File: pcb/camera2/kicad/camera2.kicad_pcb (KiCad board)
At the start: 4 copper layers, 96.5 x 45.7 mm, 63 parts

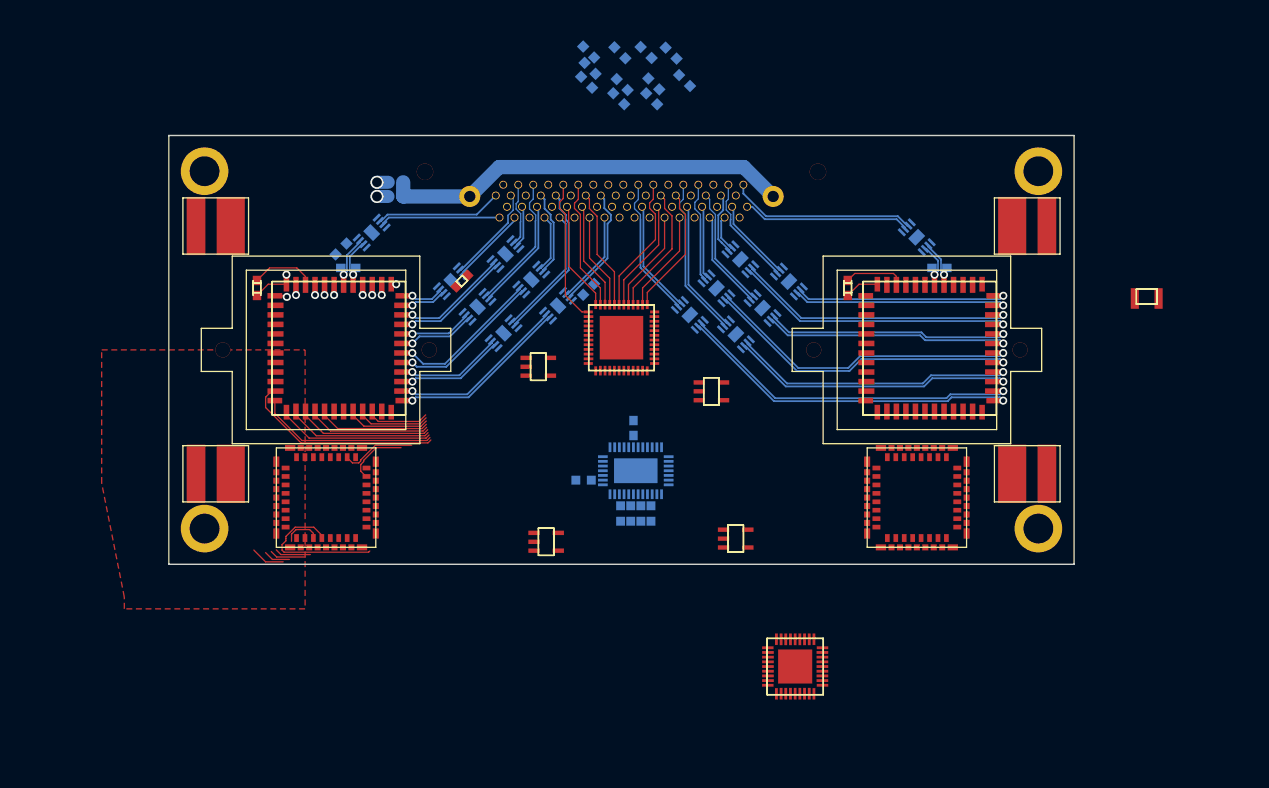
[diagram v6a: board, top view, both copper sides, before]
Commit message: moved to larger CPLD, fully routed all camera IO
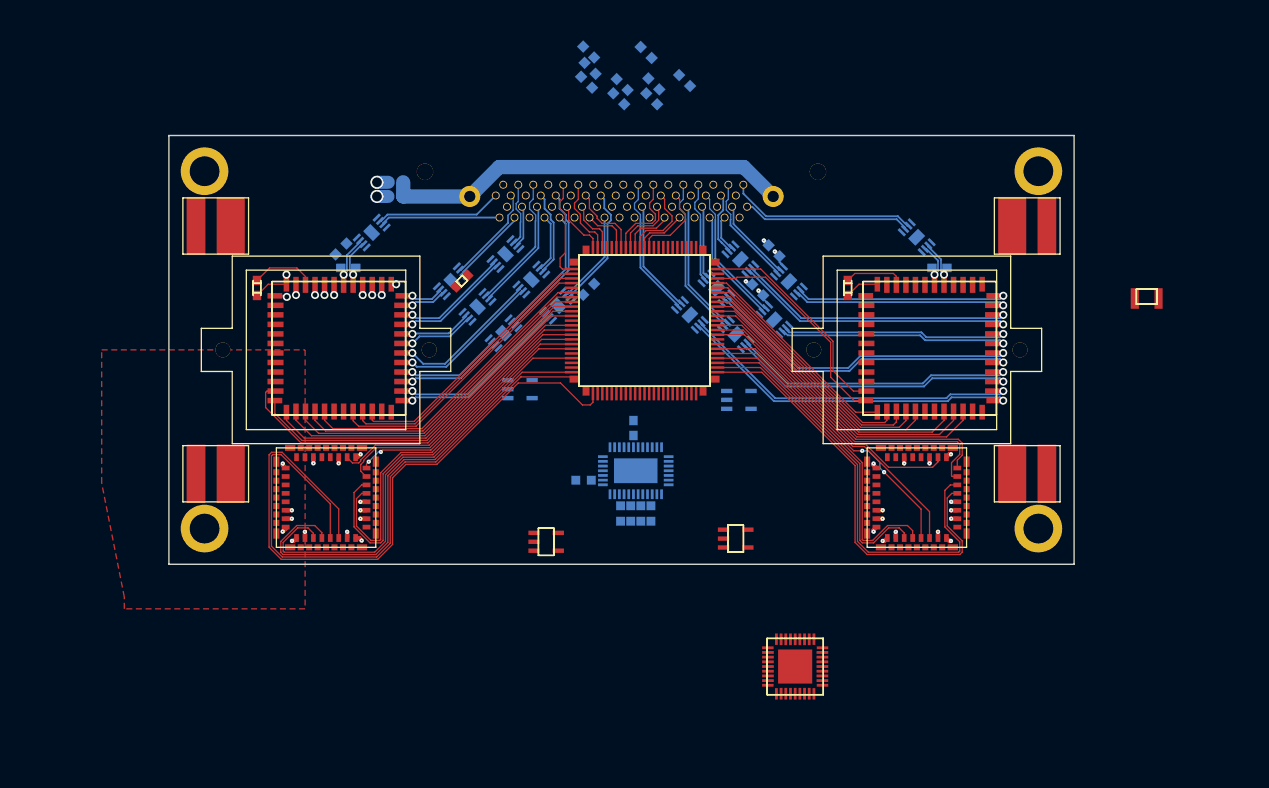
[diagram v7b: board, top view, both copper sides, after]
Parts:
- B1, B10, B11, B15, B16, B17, B18, B19, B2, B20, B3, B4, B5, B6: footprint gen:3d38d65c100b6aead619492f390645d2b3e8d681eafa555a532e446fd368cdfe -> gen:cbfca23ea51b44d0e50a3924c338fdaf501ecf837853ca0935bf710595246917
- C1U1, C2U1: footprint gen:10664f9dd6177ce506434faab979da9940bc5d6708cf5ab191b3981663e60871 -> gen:6d493ddc3734994c4679d6f237aa2fb3f74991f820373e79c6f4096ba149339f
- REG0: footprint gen:9307145be34b838094d50d6127d267a01064a34262a858c6cc372ed45fbcf923 -> gen:1903a4779b06bda6906355a6975fe99681d3728d7d24bedee3948d646425ea68; moved to B.Cu
- REG1: footprint gen:3f20292ba4d13303f6409eaa747039e0a582959419ed18ba4e4aba019cd1d96a -> gen:e735e18d7b59f93f6d8dc82e4511332583ebdf5f0f235867fb844753d55e3b85
- REG2: footprint gen:483bd425d8bab395efb60625be80c85a5fefd4678077339d4694436ec1c022e6 -> gen:592f443437e4907a136c2a8f15a046d45298603496460f15f2bf67178d41a18d; moved to B.Cu
- REG3: footprint gen:123d81daf45eb7ed1e1b6a64120b0a1dbdff9846c7f8e55397529a55efe676b0 -> gen:8bdb86a8c09f68889531c998e34d722e0e69213950ced7718ce21004f19b9346
- U1: footprint gen:e8f52075ef0fec7eeda68900a2821086d1141156e5d1efd66789b578e79d2fd0 -> gen:6cb9c5b135a5546ed2bb9661a4f4d92ab0637d7360c153991a94e593bb0a56c2
- U2: footprint gen:256d909fbafaab98513a0740e190710aa9cca955fd39664bcfd9360a469d33f3 -> gen:2b1b8886a1ea8f37823178f4470ad8a0f26e8cdd6924e7ac0c0e142e2d1baa6b
- U3: footprint gen:80313a3e577ad6f11b72c2abe74f0b6693dabd05551230f1f1f34e41c130c0e0 -> gen:c467afeea696777d1018f301cfbe94d108322fe2185f715458ad75557c396b21
- moved B17C 29.2 mm to (164.4, 92.7), turned to 135 degrees
- moved B19C 23.8 mm to (166.1, 88.5), turned to 135 degrees
- moved REG0 3.08 mm to (139.0, 103.2)
- moved REG2 3.07 mm to (162.4, 104.4)
- moved U2 3.06 mm to (152.3, 95.9)
- moved B17 1.75 mm to (166.1, 95.8)
- renumbered T1 to T1U, T2 to T2U
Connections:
- net T1_17_NC renamed T1U_17_NC
- net T1_28_MIPI_CLK_N renamed T1U_28_MIPI_CLK_N
- net T1_29_MIPI_CLK_P renamed T1U_29_MIPI_CLK_P
- net T1_2_GPIO3 renamed T1U_2_GPIO3
- net T1_31_MIPI_DATA_N renamed T1U_31_MIPI_DATA_N
- net T1_32_MIPI_DATA_P renamed T1U_32_MIPI_DATA_P
- net T1_3_GPIO2 renamed T1U_3_GPIO2
- net T1_4_GPIO1 renamed T1U_4_GPIO1
- net T1_5_GPIO0 renamed T1U_5_GPIO0
- net T2_17_NC renamed T2U_17_NC
- net T2_28_MIPI_CLK_N renamed T2U_28_MIPI_CLK_N
- net T2_29_MIPI_CLK_P renamed T2U_29_MIPI_CLK_P
- net T2_2_GPIO3 renamed T2U_2_GPIO3
- net T2_31_MIPI_DATA_N renamed T2U_31_MIPI_DATA_N
- net T2_32_MIPI_DATA_P renamed T2U_32_MIPI_DATA_P
- net T2_3_GPIO2 renamed T2U_3_GPIO2
- net T2_4_GPIO1 renamed T2U_4_GPIO1
- net T2_5_GPIO0 renamed T2U_5_GPIO0
- REG1 pad 5: vcc3_0 -> vcc1_8
- REG2 pad 5: vcc1_8 -> vcc3_0
- T1U pad 11: MOSI -> T1MOSI
- T1U pad 12: MISO -> T1MISO
- T1U pad 13: SCLK -> T1SCLK
- T1U pad 14: lepton1_cs_n -> T1_ss_n
- T1U pad 21: SCL -> T1SCL
- T1U pad 22: SDA -> T1SDA
- T1U pad 23: T1_23_PWR_DWN_L -> T1_pwr_dwn_l
- T1U pad 24: T1_24_RESET_L -> T1_reset_l
- T1U pad 26: T1_26_MASTER_CLK -> T1_master_clk
- T2U pad 11: MOSI -> T2MOSI
- T2U pad 12: MISO -> T2MISO
- T2U pad 13: SCLK -> T2SCLK
- T2U pad 14: lepton2_cs_n -> T2_ss_n
- T2U pad 21: SCL -> T2SCL
- T2U pad 22: SDA -> T2SDA
- T2U pad 23: T2_23_PWR_DWN_L -> T2_pwr_dwn_l
- T2U pad 24: T2_24_RESET_L -> T2_reset_l
- T2U pad 26: T2_26_MASTER_CLK -> T2_master_clk
- U2 pad 1: pair14N -> U2_1_IO2_1
- U2 pad 10: pair8P -> U2_10_IO2_10
- U2 pad 11: pair8N -> U2_11_IO2_11
- U2 pad 12: pair7P -> pair14N
- U2 pad 13: pair7N -> pair14P
- U2 pad 14: U2_14_IO1_14 -> pair13N
- U2 pad 15: U2_15_IO1_15 -> pair13P
- U2 pad 16: gnd -> pair12P
- U2 pad 17: U2_17_IO1_17 -> pair12N
- U2 pad 18: U2_18_IO1_18 -> pair9N
- U2 pad 19: vcc3_0 -> pair9P
- U2 pad 2: pair14P -> U2_2_IO2_2
- U2 pad 20: U2_20_IO1_20 -> vcc3_0
- U2 pad 21: cpld_TDI -> gnd
- U2 pad 22: cpld_TMS -> pair8P
- U2 pad 23: cpld_TCK -> pair8N
- U2 pad 24: U2_24_IO1_24 -> pair7P
- U2 pad 25: U2_25_IO1_25 -> gnd
- U2 pad 26: U2_26_IO1_26 -> vcc1_8
- U2 pad 27: U2_27_IO1_27 -> pair7N
- U2 pad 28: U2_28_IO1_28 -> C1SCLK
- U2 pad 29: vcc1_8 -> C1MISO
- U2 pad 3: vcc3_0 -> U2_3_IO2_3
- U2 pad 30: U2_30_IO1_30 -> C1MOSI
- U2 pad 32: U2_32_IO2_32 -> C1_ss_n
- U2 pad 33: U2_33_IO2_33 -> C1reset_n
- U2 pad 34: U2_34_IO2_34 -> C1monitor1
- U2 pad 35: U2_35_IO2_35 -> C1monitor0
- U2 pad 36: U2_36_IO2_36 -> C1trigger2
- U2 pad 37: U2_37_IO2_37 -> C1trigger1
- U2 pad 38: U2_38_IO2_38 -> vcc3_0
- U2 pad 39: U2_39_IO2_39 -> C1trigger0
- U2 pad 4: pair13N -> U2_4_IO2_4
- U2 pad 40: cpld_TDO -> T1_master_clk
- U2 pad 41: gnd -> T1_pwr_dwn_l
- U2 pad 42: vcc3_0 -> T1_reset_l
- U2 pad 43: U2_43_IO2_43 -> T1SCL
- U2 pad 44: U2_44_IO2_44 -> T1SDA
- U2 pad 45: U2_45_IO2_45 -> cpld_TDI
- U2 pad 46: U2_46_IO2_46 -> T1MOSI
- U2 pad 47: U2_47_IO2_47 -> cpld_TMS
- U2 pad 48: U2_48_IO2_48 -> cpld_TCK
- U2 pad 5: pair13P -> vcc3_0
- U2 pad 6: pair12P -> U2_6_IO2_6
- U2 pad 7: pair12N -> U2_7_IO2_7
- U2 pad 8: pair9N -> U2_8_IO2_8
- U2 pad 9: pair9P -> U2_9_IO2_9
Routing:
- net T1_ss_n: track 0.00 -> 72.1 mm
- net T1SCLK: track 0.00 -> 66.7 mm
- net T1MISO: track 0.00 -> 50.8 mm
- net T1MOSI: track 0.00 -> 49.1 mm
- net T2SDA: track 0.00 -> 47.6 mm
- net T2SCL: track 0.00 -> 46.8 mm
- net T1SDA: track 0.00 -> 42.0 mm
- net T1SCL: track 0.00 -> 40.7 mm
- net T2MISO: track 0.00 -> 35.4 mm
- net T2_pwr_dwn_l: track 0.00 -> 35.3 mm
- net T2_reset_l: track 0.00 -> 34.2 mm
- net T2MOSI: track 0.00 -> 34.1 mm
- net C2SCLK: track 0.00 -> 33.2 mm
- net T2_ss_n: track 0.00 -> 32.6 mm
- net C2MISO: track 0.00 -> 32.2 mm
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
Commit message: camera pcb: work?
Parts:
- added D0C: , gen:14fdd466f7178f17380f48cf89da463f18b4a0e8fcfb609cb3e620722c947cd3, B.Cu at (147.1, 118.2)
- added D0R: , gen:57f8f96f6e6b2a00af4539d585b2f3bdc0d73935af5ecd13a4a5208aab3df262, F.Cu at (150.4, 130.1)
- added D1C: , gen:14fdd466f7178f17380f48cf89da463f18b4a0e8fcfb609cb3e620722c947cd3, B.Cu at (153.1, 120.1)
- added D1R: , gen:57f8f96f6e6b2a00af4539d585b2f3bdc0d73935af5ecd13a4a5208aab3df262, F.Cu at (154.5, 129.9)
- added D2C: , gen:14fdd466f7178f17380f48cf89da463f18b4a0e8fcfb609cb3e620722c947cd3, B.Cu at (150.4, 120.2)
- added D2R: , gen:57f8f96f6e6b2a00af4539d585b2f3bdc0d73935af5ecd13a4a5208aab3df262, F.Cu at (152.2, 128.6)
- added D3C: , gen:14fdd466f7178f17380f48cf89da463f18b4a0e8fcfb609cb3e620722c947cd3, B.Cu at (147.4, 120.1)
- added D3R: , gen:57f8f96f6e6b2a00af4539d585b2f3bdc0d73935af5ecd13a4a5208aab3df262, F.Cu at (150.2, 131.7)
- B1, B10, B11, B15, B16, B17, B18, B19, B2, B20, B3, B4, B5, B6: footprint gen:cbfca23ea51b44d0e50a3924c338fdaf501ecf837853ca0935bf710595246917 -> gen:b84940fdfb16a2d7942b3b406dd98b10c2c2213999c6866e353299b244b8fc6e
- C1U1, C2U1: footprint gen:6d493ddc3734994c4679d6f237aa2fb3f74991f820373e79c6f4096ba149339f -> gen:d5f9e289ee2336b21afcfae927cf410e4925b1050bf518abb5cf178e2b219273
- REG0: footprint gen:1903a4779b06bda6906355a6975fe99681d3728d7d24bedee3948d646425ea68 -> gen:1add349ebd9963d752faf6d62c14ce67e4cb2b1431c56764e8a0fc8115b29539
- REG1: footprint gen:e735e18d7b59f93f6d8dc82e4511332583ebdf5f0f235867fb844753d55e3b85 -> gen:301270a8d4f2b83b7524f9f1e316186f15d4407ffff898fc97f7a9bf814ba95e
- REG2: footprint gen:592f443437e4907a136c2a8f15a046d45298603496460f15f2bf67178d41a18d -> gen:3dff63c1257816c390bd930d4e9e2a3d002c3804d7440e0068ce39245183ded9
- REG3: footprint gen:8bdb86a8c09f68889531c998e34d722e0e69213950ced7718ce21004f19b9346 -> gen:fab45f821aaed4b2e2c106769317244450312030644283560206288729765279
- U1: footprint gen:6cb9c5b135a5546ed2bb9661a4f4d92ab0637d7360c153991a94e593bb0a56c2 -> gen:0306e6b5f641219b29c97fb93a4bb6fb11c91cc1b6f63197c18a4913509fb757
- U3: footprint gen:c467afeea696777d1018f301cfbe94d108322fe2185f715458ad75557c396b21 -> gen:7dbf8df50efd715a448db095119b3b26608df54065546b11197adccbe633bb61
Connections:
- U3 pad 10: cap3 -> vcc5in
- U3 pad 3: cap0 -> vcc5in
- U3 pad 4: cap1 -> vcc5in
- U3 pad 9: cap2 -> vcc5in
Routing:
- net vcc3_3in: track 3.99 -> 6.71 mm
